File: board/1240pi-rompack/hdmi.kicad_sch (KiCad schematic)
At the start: 3 parts, among them J1 HDMI_A, J2 HDMI_A

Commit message: Update board license to CERN-OHL-S v2+.
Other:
- company: (none) -> © 2022 Sam Hanes, licensed under CERN-OHL-S v2+
- title: (none) -> 1240-Pi ROM Pack
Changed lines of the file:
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@@
 (kicad_sch (version 20211123) (generator eeschema)
-  (paper "A4")
+  (paper "USLetter")
+  (title_block
+    (title "1240-Pi ROM Pack")
+    (date "2022-05-21")
+    (rev "1.0")
+    (company "© 2022 Sam Hanes, licensed under CERN-OHL-S v2+")
+    (comment 1 "https://github.com/Elemecca/1240pi")
+  )
   (junction (at 256.54 81.28) (diameter 0) (color 0 0 0 0)
   )
@@
       (effects (font (size 1.27 1.27)) hide)
     )
+    (pin "1")
+    (pin "100")
+    (pin "107")
+    (pin "108")
+    (pin "113")
+    (pin "114")
+    (pin "119")
+    (pin "120")
+    (pin "125")
+    (pin "126")
+    (pin "13")
+    (pin "131")
+    (pin "132")
+    (pin "137")
+    (pin "138")
+    (pin "14")
+    (pin "144")
+    (pin "150")
+    (pin "155")
+    (pin "156")
+    (pin "161")
+    (pin "162")
+    (pin "167")
+    (pin "168")
+    (pin "173")
+    (pin "174")
+    (pin "179")
+    (pin "180")
+    (pin "185")
+    (pin "186")
+    (pin "191")
+    (pin "192")
+    (pin "197")
+    (pin "198")
+    (pin "2")
+    (pin "20")
+    (pin "21")
+    (pin "22")
+    (pin "23")
+    (pin "32")
+    (pin "33")
+    (pin "42")
+    (pin "43")
+    (pin "52")
+    (pin "53")
+    (pin "59")
+    (pin "60")
+    (pin "65")
+    (pin "66")
+    (pin "7")
+    (pin "71")
+    (pin "74")
+    (pin "77")
+    (pin "79")
+    (pin "8")
+    (pin "81")
+    (pin "83")
+    (pin "84")
+    (pin "85")
+    (pin "86")
+    (pin "87")
+    (pin "88")
+    (pin "89")
+    (pin "90")
+    (pin "91")
+    (pin "92")
+    (pin "93")
+    (pin "95")
+    (pin "98")
+    (pin "99")
+    (pin "10")
+    (pin "11")
+    (pin "12")
+    (pin "15")
+    (pin "16")
+    (pin "17")
+    (pin "18")
+    (pin "19")
+    (pin "3")
+    (pin "4")
+    (pin "5")
+    (pin "6")
+    (pin "9")
+    (pin "24")
+    (pin "25")
+    (pin "26")
+    (pin "27")
+    (pin "28")
+    (pin "29")
+    (pin "30")
+    (pin "31")
+    (pin "34")
+    (pin "35")
+    (pin "36")
+    (pin "37")
+    (pin "38")
+    (pin "39")
+    (pin "40")
+    (pin "41")
+    (pin "44")
+    (pin "45")
+    (pin "46")
+    (pin "47")
+    (pin "48")
+    (pin "49")
+    (pin "50")
+    (pin "51")
+    (pin "54")
+    (pin "55")
+    (pin "56")
+    (pin "58")
+    (pin "78")
+    (pin "57")
+    (pin "61")
+    (pin "62")
+    (pin "63")
+    (pin "64")
+    (pin "67")
+    (pin "68")
+    (pin "69")
+    (pin "70")
+    (pin "72")
+    (pin "73")
+    (pin "75")
+    (pin "101")
+    (pin "103")
+    (pin "105")
+    (pin "94")
+    (pin "96")
+    (pin "102")
+    (pin "109")
+    (pin "110")
+    (pin "112")
+    (pin "116")
+    (pin "118")
+    (pin "122")
+    (pin "124")
+    (pin "104")
+    (pin "106")
+    (pin "111")
+    (pin "115")
+    (pin "117")
+    (pin "121")
+    (pin "123")
+    (pin "127")
+    (pin "128")
+    (pin "129")
+    (pin "130")
+    (pin "133")
+    (pin "134")
+    (pin "135")
+    (pin "136")
+    (pin "139")
+    (pin "140")
+    (pin "141")
+    (pin "142")
+    (pin "157")
+    (pin "159")
+    (pin "163")
+    (pin "165")
+    (pin "169")
+    (pin "171")
+    (pin "175")
+    (pin "177")
+    (pin "181")
+    (pin "183")
+    (pin "187")
+    (pin "189")
+    (pin "193")
+    (pin "194")
+    (pin "195")
+    (pin "196")
+    (pin "76")
+    (pin "80")
+    (pin "82")
+    (pin "97")
     (pin "143")
     (pin "145")

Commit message: Add more stuff to rompack board.
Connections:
- net HDMI_OUT_D2_P: now reaches J2.1 (D2+)
- net HDMI_OUT_D2_P: now also A1.146 (HDMI1_TX2_P)
- net HDMI_OUT_CK_P: now reaches J2.10 (CK+)
- net HDMI_OUT_CK_P: now also A1.164 (HDMI1_CLK_P)
- net HDMI_OUT_CK_N: now reaches J2.12 (CK-)
- net HDMI_OUT_CK_N: now also A1.166 (HDMI1_CLK_N)
- net HDMI_OUT_CEC: now reaches J2.13 (CEC)
- net HDMI_OUT_CEC: now also A1.149 (HDMI1_CEC)
- net HDMI_OUT_SCL: now reaches J2.15 (SCL)
- net HDMI_OUT_SCL: now also A1.147 (HDMI1_SCL)
- net HDMI_OUT_SDA: now reaches J2.16 (SDA)
- net HDMI_OUT_SDA: now also A1.145 (HDMI1_SDA)
- net HDMI_OUT_+5V: now reaches J2.18 (+5V)
- net HDMI_OUT_HPD: now reaches J2.19 (HPD)
- net HDMI_OUT_HPD: now also A1.143 (HDMI1_HOTPLUG)
- net HDMI_OUT_D2_N: now reaches J2.3 (D2-)
- net HDMI_OUT_D2_N: now also A1.148 (HDMI1_TX2_N)
- net HDMI_OUT_D1_P: now reaches J2.4 (D1+)
- net HDMI_OUT_D1_P: now also A1.152 (HDMI1_TX1_P)
- net HDMI_OUT_D1_N: now reaches J2.6 (D1-)
- net HDMI_OUT_D1_N: now also A1.154 (HDMI1_TX1_N)
- net HDMI_OUT_D0_P: now reaches J2.7 (D0+)
- net HDMI_OUT_D0_P: now also A1.158 (HDMI1_TX0_P)
- net HDMI_OUT_D0_N: now reaches J2.9 (D0-)
- net HDMI_OUT_D0_N: now also A1.160 (HDMI1_TX0_N)
- net HDMI_IN_D2_P: now reaches J1.1 (D2+)
- net HDMI_IN_CK_P: now reaches J1.10 (CK+)
- net HDMI_IN_CK_N: now reaches J1.12 (CK-)
- net HDMI_IN_CEC: now reaches J1.13 (CEC)
- net HDMI_IN_SCL: now reaches J1.15 (SCL)
- net HDMI_IN_SDA: now reaches J1.16 (SDA)
- net HDMI_IN_HPD: now reaches J1.19 (HPD)
- net HDMI_IN_D2_N: now reaches J1.3 (D2-)
- net HDMI_IN_D1_P: now reaches J1.4 (D1+)
- net HDMI_IN_D1_N: now reaches J1.6 (D1-)
- net HDMI_IN_D0_P: now reaches J1.7 (D0+)
- net HDMI_IN_D0_N: now reaches J1.9 (D0-)
- no-connect marks 0 -> 2
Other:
- moved on the sheet: J1, J2

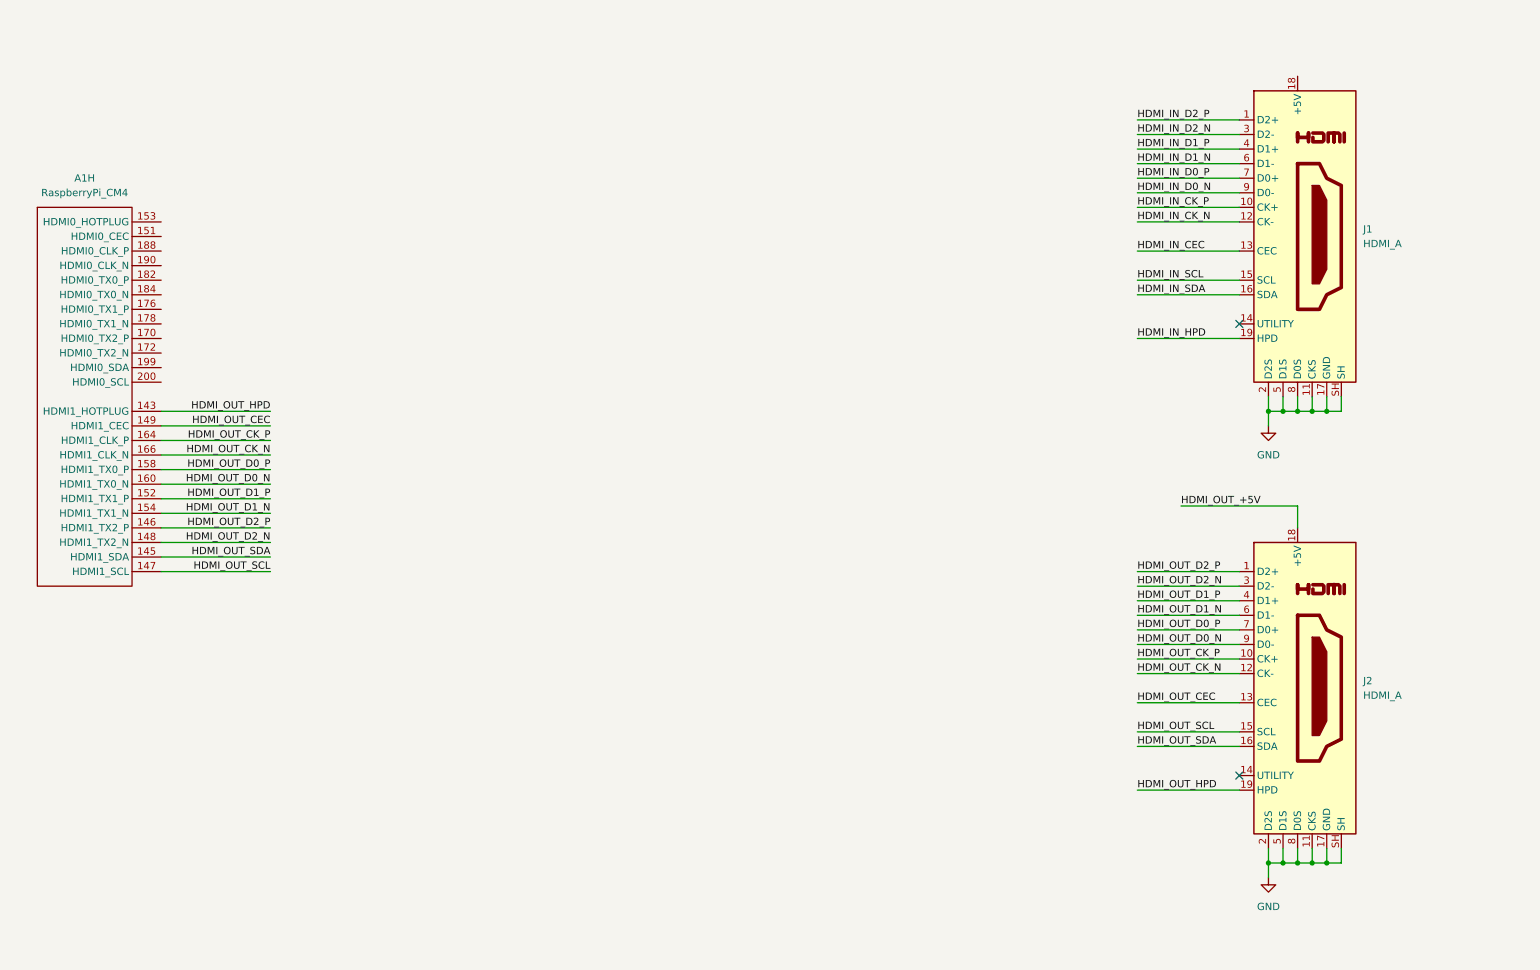
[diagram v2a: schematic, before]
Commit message: Split connectors out of CM4 footprint.
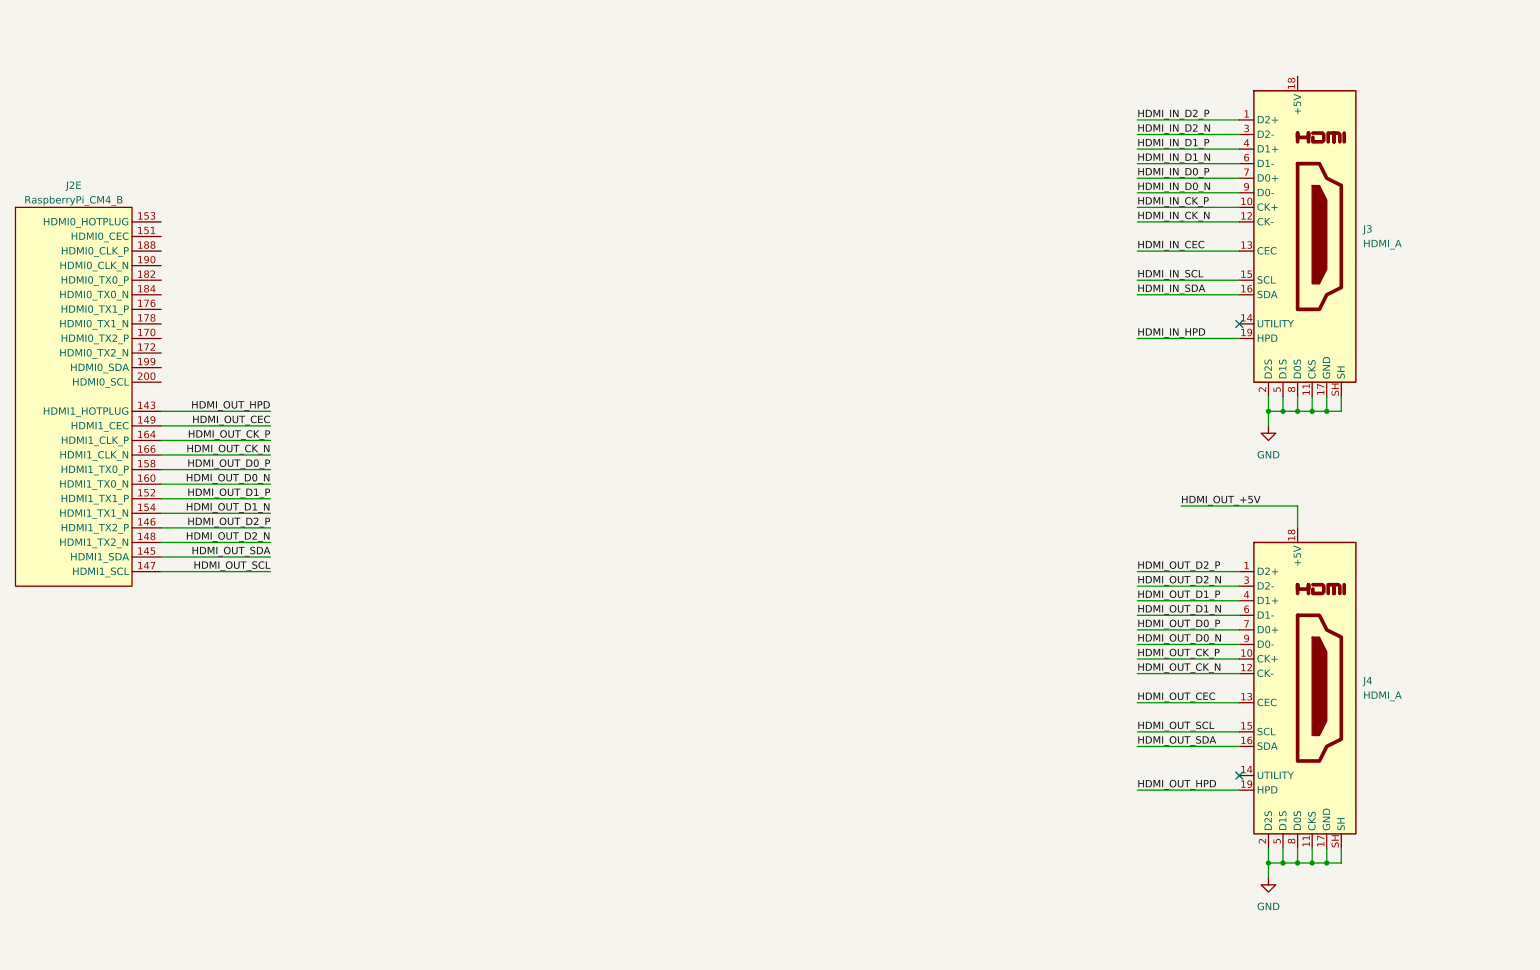
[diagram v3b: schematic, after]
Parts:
- removed A1: RaspberryPi_CM4, 0Local:RaspberryPi_CM4, symbol 0Local:RaspberryPi_CM4
- added J2: RaspberryPi_CM4_B, 0Local:Hirose_DF40C-100DS-0.4V, symbol 0Local:RaspberryPi_CM4_B
- renumbered J1 to J3, J2 to J4
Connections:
- net HDMI_OUT_CEC: now also J2.149 (HDMI1_CEC)
- net HDMI_OUT_CK_N: now also J2.166 (HDMI1_CLK_N)
- net HDMI_OUT_CK_P: now also J2.164 (HDMI1_CLK_P)
- net HDMI_OUT_D0_N: now also J2.160 (HDMI1_TX0_N)
- net HDMI_OUT_D0_P: now also J2.158 (HDMI1_TX0_P)
- net HDMI_OUT_D1_N: now also J2.154 (HDMI1_TX1_N)
- net HDMI_OUT_D1_P: now also J2.152 (HDMI1_TX1_P)
- net HDMI_OUT_D2_N: now also J2.148 (HDMI1_TX2_N)
- net HDMI_OUT_D2_P: now also J2.146 (HDMI1_TX2_P)
- net HDMI_OUT_HPD: now also J2.143 (HDMI1_HOTPLUG)
- net HDMI_OUT_SCL: now also J2.147 (HDMI1_SCL)
- net HDMI_OUT_SDA: now also J2.145 (HDMI1_SDA)
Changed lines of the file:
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@@
     (pin "1")
   )
-  (symbol (lib_id "Connector:HDMI_A") (at 241.3 139.7 0) (unit 1)
-    (in_bom yes) (on_board yes) (fields_autoplaced)
-    (property "Reference" "J2" (id 0) (at 252.73 138.4299 0)
-      (effects (font (size 1.27 1.27)) (justify left))
-    )
-    (property "Value" "HDMI_A" (id 1) (at 252.73 140.9699 0)
-      (effects (font (size 1.27 1.27)) (justify left))
-    )
-    (property "Footprint" "0Local:CNC_2000-1-2-41-00-BK" (id 2) (at 241.935 139.7 0)
+  (symbol (lib_id "0Local:RaspberryPi_CM4_B") (at 27.94 55.88 0) (unit 5)
+    (in_bom yes) (on_board yes)
+    (property "Reference" "J2" (id 0) (at 27.94 52.07 0))
+    (property "Value" "RaspberryPi_CM4_B" (id 1) (at 27.94 54.61 0))
+    (property "Footprint" "0Local:Hirose_DF40C-100DS-0.4V" (id 2) (at 27.94 49.53 0)
       (effects (font (size 1.27 1.27)) hide)
     )
-    (property "Datasheet" "https://en.wikipedia.org/wiki/HDMI" (id 3) (at 241.935 139.7 0)
+    (property "Datasheet" "https://datasheets.raspberrypi.com/cm4/cm4-datasheet.pdf" (id 3) (at 27.94 46.99 0)
       (effects (font (size 1.27 1.27)) hide)
     )
-    (pin "1")
-    (pin "10")
-    (pin "11")
-    (pin "12")
-    (pin "13")
-    (pin "14")
-    (pin "15")
-    (pin "16")
-    (pin "17")
-    (pin "18")
-    (pin "19")
-    (pin "2")
-    (pin "3")
-    (pin "4")
-    (pin "5")
-    (pin "6")
-    (pin "7")
-    (pin "8")
-    (pin "9")
-    (pin "SH")
-  )
-  (symbol (lib_id "Connector:HDMI_A") (at 241.3 60.96 0) (unit 1)
-    (in_bom yes) (on_board yes) (fields_autoplaced)
-    (property "Reference" "J1" (id 0) (at 252.73 59.6899 0)
-      (effects (font (size 1.27 1.27)) (justify left))
-    )
-    (property "Value" "HDMI_A" (id 1) (at 252.73 62.2299 0)
-      (effects (font (size 1.27 1.27)) (justify left))
-    )
-    (property "Footprint" "0Local:CNC_2000-1-2-41-00-BK" (id 2) (at 241.935 60.96 0)
-      (effects (font (size 1.27 1.27)) hide)
-    )
-    (property "Datasheet" "https://en.wikipedia.org/wiki/HDMI" (id 3) (at 241.935 60.96 0)
-      (effects (font (size 1.27 1.27)) hide)
-    )
-    (pin "1")
-    (pin "10")
-    (pin "11")
-    (pin "12")
-    (pin "13")
-    (pin "14")
-    (pin "15")
-    (pin "16")
-    (pin "17")
-    (pin "18")
-    (pin "19")
-    (pin "2")
-    (pin "3")
-    (pin "4")
-    (pin "5")
-    (pin "6")
-    (pin "7")
-    (pin "8")
-    (pin "9")
-    (pin "SH")
-  )
-  (symbol (lib_id "0Local:RaspberryPi_CM4") (at 21.59 58.42 0) (unit 8)
-    (in_bom yes) (on_board yes) (fields_autoplaced)
-    (property "Reference" "A1" (id 0) (at 29.845 50.8 0))
-    (property "Value" "RaspberryPi_CM4" (id 1) (at 29.845 53.34 0))
-    (property "Footprint" "0Local:RaspberryPi_CM4" (id 2) (at 21.59 82.55 0)
-      (effects (font (size 1.27 1.27)) hide)
-    )
-    (property "Datasheet" "" (id 3) (at 16.51 58.42 0)
-      (effects (font (size 1.27 1.27)) hide)
-    )
-    (pin "1")
-    (pin "100")
     (pin "107")
     (pin "108")
@@
     (pin "125")
     (pin "126")
-    (pin "13")
     (pin "131")
     (pin "132")
     (pin "137")
     (pin "138")
-    (pin "14")
     (pin "144")
     (pin "150")
@@
     (pin "197")
     (pin "198")
-    (pin "2")
-    (pin "20")
-    (pin "21")
-    (pin "22")
-    (pin "23")
-    (pin "32")
-    (pin "33")
-    (pin "42")
-    (pin "43")
-    (pin "52")
-    (pin "53")
-    (pin "59")
-    (pin "60")
-    (pin "65")
-    (pin "66")
-    (pin "7")
-    (pin "71")
-    (pin "74")
-    (pin "77")
-    (pin "79")
-    (pin "8")
-    (pin "81")
-    (pin "83")
-    (pin "84")
-    (pin "85")
-    (pin "86")
-    (pin "87")
-    (pin "88")
-    (pin "89")
-    (pin "90")
-    (pin "91")
-    (pin "92")
-    (pin "93")
-    (pin "95")
-    (pin "98")
-    (pin "99")
-    (pin "10")
-    (pin "11")
-    (pin "12")
-    (pin "15")
-    (pin "16")
-    (pin "17")
-    (pin "18")
-    (pin "19")
-    (pin "3")
-    (pin "4")
-    (pin "5")
-    (pin "6")
-    (pin "9")
-    (pin "24")
-    (pin "25")
-    (pin "26")
-    (pin "27")
-    (pin "28")
-    (pin "29")
-    (pin "30")
-    (pin "31")
-    (pin "34")
-    (pin "35")
-    (pin "36")
-    (pin "37")
-    (pin "38")
-    (pin "39")
-    (pin "40")
-    (pin "41")
-    (pin "44")
-    (pin "45")
-    (pin "46")
-    (pin "47")
-    (pin "48")
-    (pin "49")
-    (pin "50")
-    (pin "51")
-    (pin "54")
-    (pin "55")
-    (pin "56")
-    (pin "58")
-    (pin "78")
-    (pin "57")
-    (pin "61")
-    (pin "62")
-    (pin "63")
-    (pin "64")
-    (pin "67")
-    (pin "68")
-    (pin "69")
-    (pin "70")
-    (pin "72")
-    (pin "73")
-    (pin "75")
     (pin "101")
     (pin "103")
     (pin "105")
-    (pin "94")
-    (pin "96")
     (pin "102")
     (pin "109")
@@
     (pin "195")
     (pin "196")
-    (pin "76")
-    (pin "80")
-    (pin "82")
-    (pin "97")
     (pin "143")
     (pin "145")
@@
     (pin "200")
   )
+  (symbol (lib_id "Connector:HDMI_A") (at 241.3 139.7 0) (unit 1)
+    (in_bom yes) (on_board yes) (fields_autoplaced)
+    (property "Reference" "J4" (id 0) (at 252.73 138.4299 0)
+      (effects (font (size 1.27 1.27)) (justify left))
+    )
+    (property "Value" "HDMI_A" (id 1) (at 252.73 140.9699 0)
+      (effects (font (size 1.27 1.27)) (justify left))
+    )
+    (property "Footprint" "0Local:CNC_2000-1-2-41-00-BK" (id 2) (at 241.935 139.7 0)
+      (effects (font (size 1.27 1.27)) hide)
+    )
+    (property "Datasheet" "https://en.wikipedia.org/wiki/HDMI" (id 3) (at 241.935 139.7 0)
+      (effects (font (size 1.27 1.27)) hide)
+    )
+    (pin "1")
+    (pin "10")
+    (pin "11")
+    (pin "12")
+    (pin "13")
+    (pin "14")
+    (pin "15")
+    (pin "16")
+    (pin "17")
+    (pin "18")
+    (pin "19")
+    (pin "2")
+    (pin "3")
+    (pin "4")
+    (pin "5")
+    (pin "6")
+    (pin "7")
+    (pin "8")
+    (pin "9")
+    (pin "SH")
+  )
+  (symbol (lib_id "Connector:HDMI_A") (at 241.3 60.96 0) (unit 1)
+    (in_bom yes) (on_board yes) (fields_autoplaced)
+    (property "Reference" "J3" (id 0) (at 252.73 59.6899 0)
+      (effects (font (size 1.27 1.27)) (justify left))
+    )
+    (property "Value" "HDMI_A" (id 1) (at 252.73 62.2299 0)
+      (effects (font (size 1.27 1.27)) (justify left))
+    )
+    (property "Footprint" "0Local:CNC_2000-1-2-41-00-BK" (id 2) (at 241.935 60.96 0)
+      (effects (font (size 1.27 1.27)) hide)
+    )
+    (property "Datasheet" "https://en.wikipedia.org/wiki/HDMI" (id 3) (at 241.935 60.96 0)
+      (effects (font (size 1.27 1.27)) hide)
+    )
+    (pin "1")
+    (pin "10")
+    (pin "11")
+    (pin "12")
+    (pin "13")
+    (pin "14")
+    (pin "15")
+    (pin "16")
+    (pin "17")
+    (pin "18")
+    (pin "19")
+    (pin "2")
+    (pin "3")
+    (pin "4")
+    (pin "5")
+    (pin "6")
+    (pin "7")
+    (pin "8")
+    (pin "9")
+    (pin "SH")
+  )
   (symbol (lib_id "power:GND") (at 236.22 172.72 0) (unit 1)

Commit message: Route HDMI output port.
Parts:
- renumbered J4 to J3, J3 to J4
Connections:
- net HDMI_OUT_CEC: now also J2.51 (HDMI0_CEC); no longer J2.149 (HDMI1_CEC)
- net HDMI_OUT_CK_N: now also J2.90 (HDMI0_CLK_N); no longer J2.166 (HDMI1_CLK_N)
- net HDMI_OUT_CK_P: now also J2.88 (HDMI0_CLK_P); no longer J2.164 (HDMI1_CLK_P)
- net HDMI_OUT_D0_N: now also J2.84 (HDMI0_TX0_N); no longer J2.160 (HDMI1_TX0_N)
- net HDMI_OUT_D0_P: now also J2.82 (HDMI0_TX0_P); no longer J2.158 (HDMI1_TX0_P)
- net HDMI_OUT_D1_N: now also J2.78 (HDMI0_TX1_N); no longer J2.154 (HDMI1_TX1_N)
- net HDMI_OUT_D1_P: now also J2.76 (HDMI0_TX1_P); no longer J2.152 (HDMI1_TX1_P)
- net HDMI_OUT_D2_N: now also J2.72 (HDMI0_TX2_N); no longer J2.148 (HDMI1_TX2_N)
- net HDMI_OUT_D2_P: now also J2.70 (HDMI0_TX2_P); no longer J2.146 (HDMI1_TX2_P)
- net HDMI_OUT_HPD: now also J2.53 (HDMI0_HOTPLUG); no longer J2.143 (HDMI1_HOTPLUG)
- net HDMI_OUT_SCL: now also J2.100 (HDMI0_SCL); no longer J2.147 (HDMI1_SCL)
- net HDMI_OUT_SDA: now also J2.99 (HDMI0_SDA); no longer J2.145 (HDMI1_SDA)
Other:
- moved on the sheet: J2E, J3, J4
